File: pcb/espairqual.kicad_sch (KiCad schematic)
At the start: 29 parts, among them J1 24VAC, J2 PMSX003, J7 eflashy32, U1 BD9G101G, U2 ESP32-S2-WROVER, U3 AP1117-33

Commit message: hmm
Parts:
- added J3: USB_C_Receptacle_USB2.0, Connector_USB:USB_C_Receptacle_HRO_TYPE-C-31-M-12, symbol Connector:USB_C_Receptacle_USB2.0
- added R4, R7: 5k1, Resistor_SMD:R_0805_2012Metric, symbol Device:R_Small
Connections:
- net +5V: now also J3.A4 (VBUS), J3.A9 (VBUS), J3.B4 (VBUS), J3.B9 (VBUS)
- net GND: now also J3.A1 (GND), J3.A12 (GND), J3.B1 (GND), J3.B12 (GND), R4.2, R7.2
- new net: J3.A5 (CC1), R4.1
- new net: J3.B5 (CC2), R7.1
- no-connect marks 31 -> 38
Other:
- note added: "Alternate 5VDC Source"

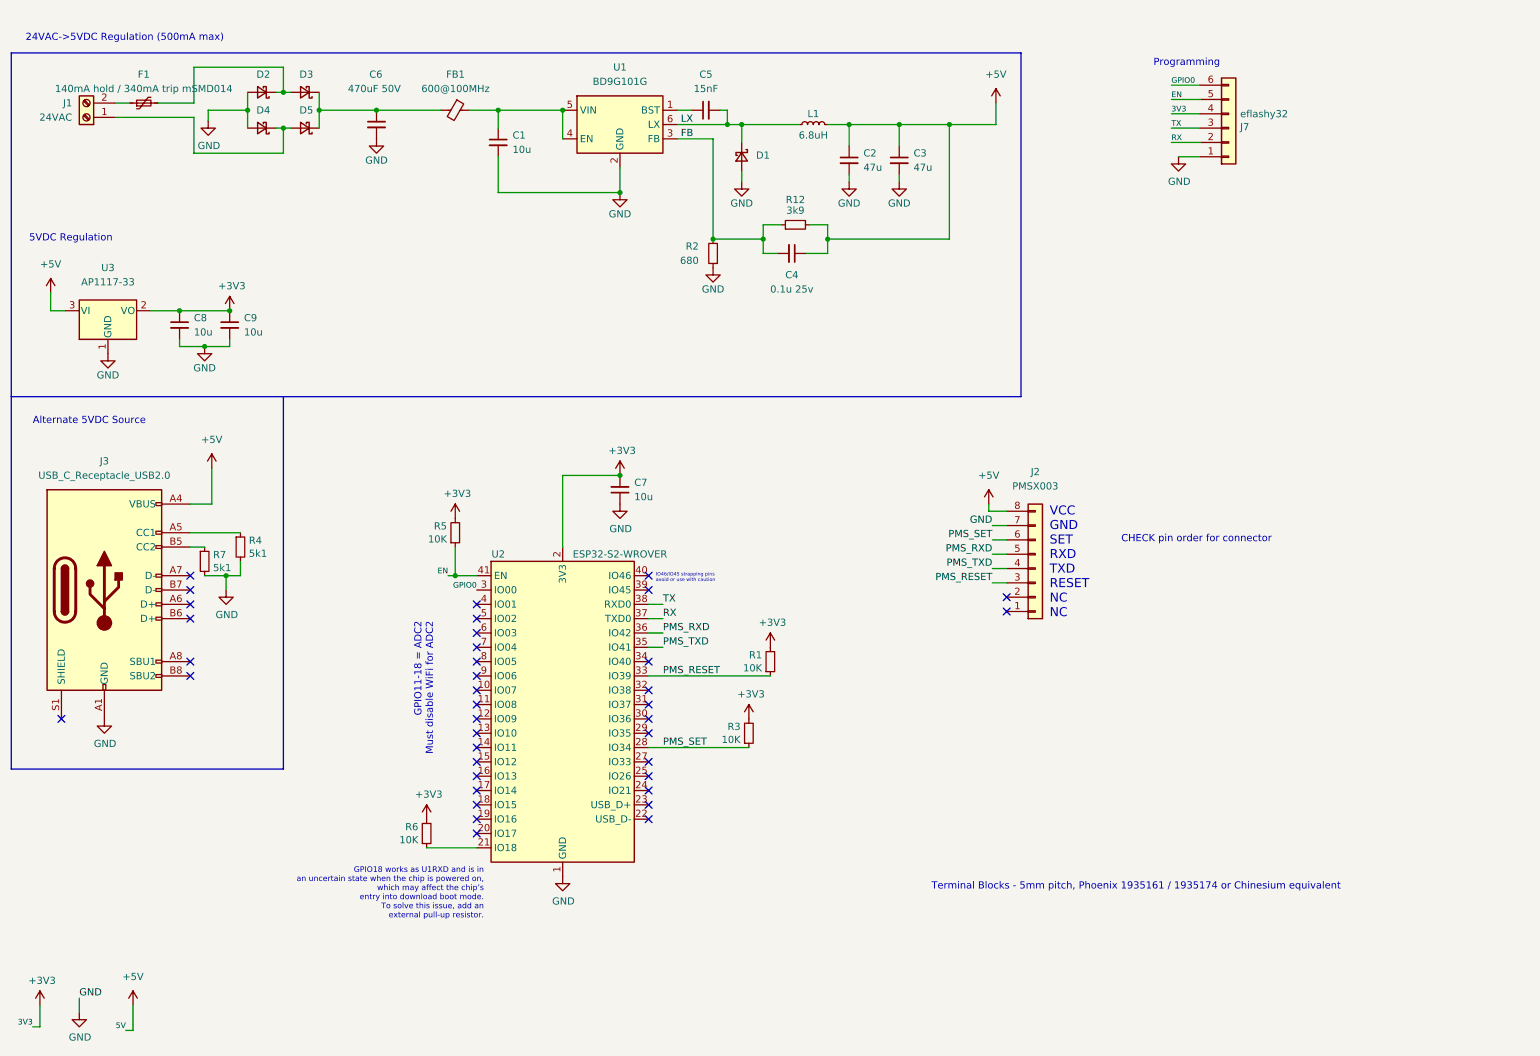
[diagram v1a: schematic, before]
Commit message: esp32 time
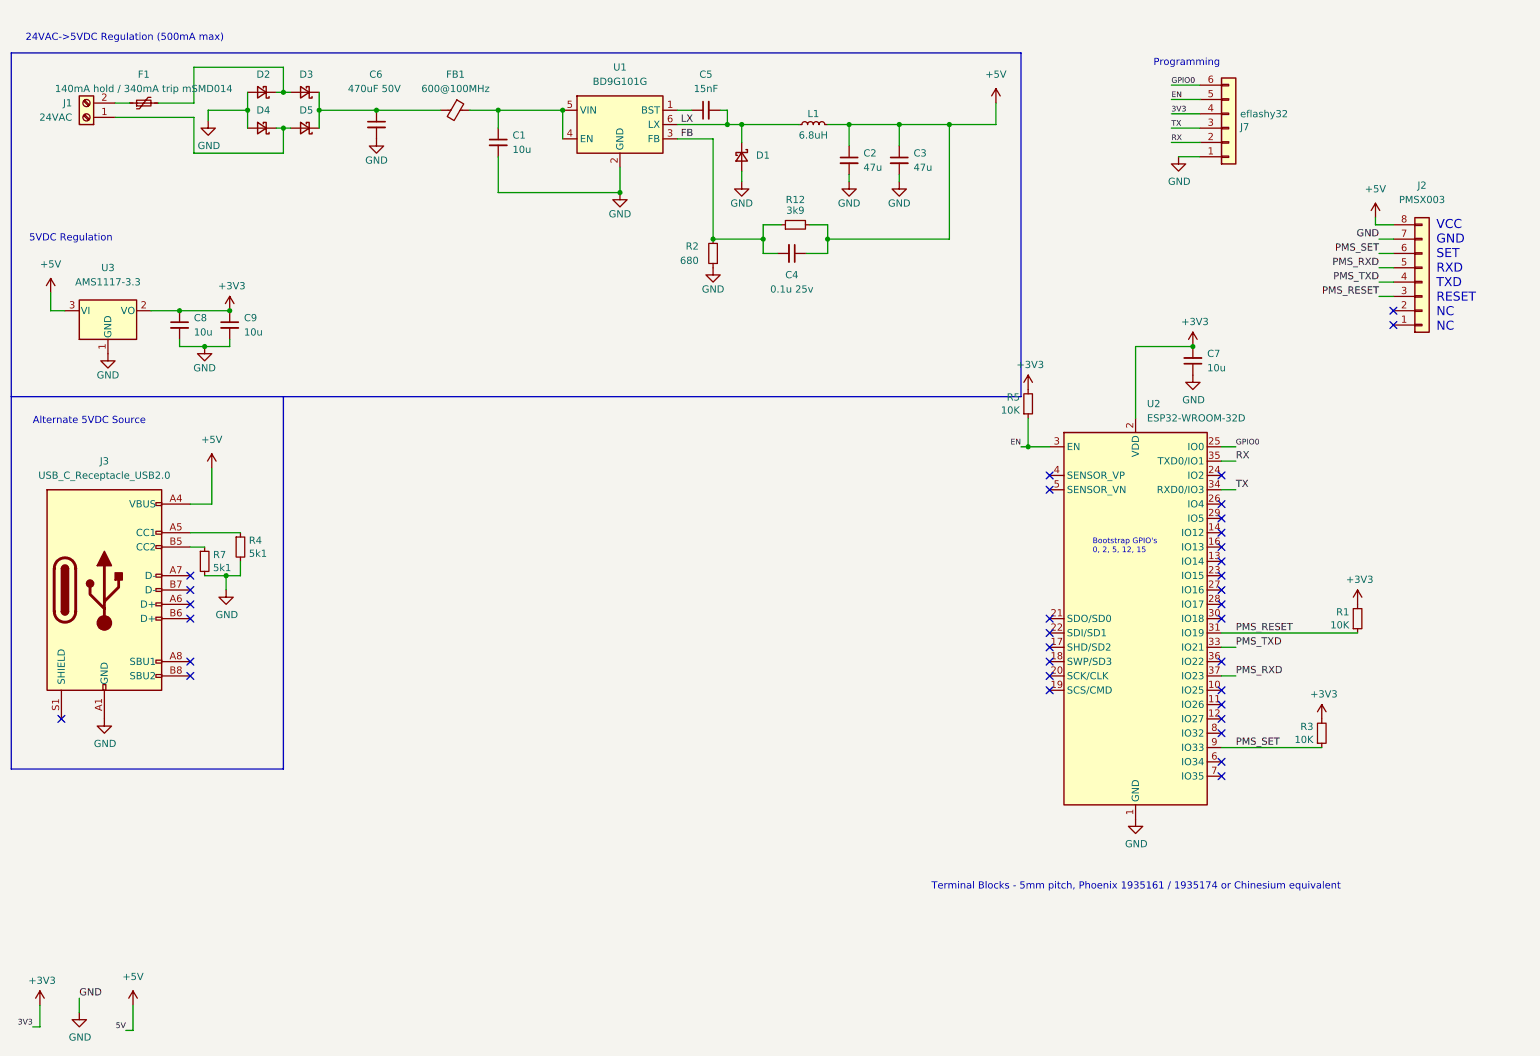
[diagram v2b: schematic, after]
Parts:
- removed R6: 10K, Resistor_SMD:R_0805_2012Metric, symbol Device:R_Small
- removed U2: ESP32-S2-WROVER, RF_Module:ESP32-S2-WROVER, symbol RF_Module:ESP32-S2-WROVER
- added U2: ESP32-WROOM-32D, RF_Module:ESP32-WROOM-32, symbol RF_Module:ESP32-WROOM-32D
- J1: LCSC a -> DNP
- J7: LCSC (none) -> DNP
- R1, R3, R5: footprint Resistor_SMD:R_0805_2012Metric -> Resistor_SMD:R_0402_1005Metric; LCSC C17414 -> C25086
- R12: footprint Resistor_SMD:R_0603_1608Metric -> Resistor_SMD:R_0402_1005Metric; LCSC C114616 -> C51721
- R2: footprint Resistor_SMD:R_0603_1608Metric -> Resistor_SMD:R_0402_1005Metric; LCSC C23228 -> C25130
- R4, R7: footprint Resistor_SMD:R_0805_2012Metric -> Resistor_SMD:R_0402_1005Metric; LCSC C27834 -> C25905
- U3: value AP1117-33 -> AMS1117-3.3; LCSC (none) -> C6186
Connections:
- net +3V3: now also U2.2 (VDD)
- net EN: now also U2.3 (EN)
- net GND: now also U2.1 (GND), U2.15 (GND), U2.38 (GND), U2.39 (GND)
- net GPIO0: now also U2.25 (IO0)
- net PMS_RESET: now also U2.31 (IO19)
- net PMS_RXD: now also U2.37 (IO23)
- net PMS_SET: now also U2.9 (IO33)
- net PMS_TXD: now also U2.33 (IO21)
- net RX: now also U2.35 (TXD0/IO1)
- net TX: now also U2.34 (RXD0/IO3)
- no-connect marks 38 -> 34
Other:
- note added: "Bootstrap GPIO's 0, 2, 5, 12, 15"
- note removed: "CHECK pin order for connector"
- note removed: "GPIO11-18 = ADC2 Must disable WiFi for ADC2"
- note removed: "GPIO18 works as U1RXD and is in an uncertain state when the chip is powered on, which may affect the chip’s entry into download boot mode. To solve this issue, add an external pull-up resistor."
- note removed: "IO46/IO45 strapping pins avoid or use with caution"
- moved on the sheet: C7, J2, R5

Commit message: caps
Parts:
- added C10, C11, C12: 10uF 50V, Capacitor_SMD:C_1206_3216Metric, symbol Device:C_Small
- C6: value 470uF 50V -> 10uF 50V; footprint Capacitor_SMD:CP_Elec_10x10 -> Capacitor_SMD:C_1206_3216Metric; LCSC C125977 -> C13585
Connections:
- net GND: now also C10.2, C11.2, C12.2
- net Vrec: now reaches C6.1, D3.1 (K), D5.1 (K), FB1.2
- net Vrec: now also C10.1, C11.1, C12.1
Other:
- moved on the sheet: FB1

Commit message: update workflow
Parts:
- removed C10, C11, C12: 10uF 50V, Capacitor_SMD:C_1206_3216Metric, symbol Device:C_Small
- added C10: 100uF 50V, Capacitor_THT:CP_Radial_D10.0mm_P5.00mm_P7.50mm, symbol Device:C_Polarized_Small
- added C16: 1uF, Capacitor_SMD:C_0603_1608Metric, symbol Device:C_Small
- added H1, H2, H3, H4: MountingHole, MountingHole:MountingHole_3.2mm_M3, symbol Mechanical:MountingHole
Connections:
- net EN: now also C16.2
- net GND: now also C10.2, C16.1
- net Vrec: now also C10.1
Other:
- moved on the sheet: C6

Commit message: changes
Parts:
- removed C16: 1uF, Capacitor_SMD:C_0603_1608Metric, symbol Device:C_Small
- removed C2, C3: 47u, Capacitor_SMD:C_1206_3216Metric, symbol Device:C_Small
- removed J3: USB_C_Receptacle_USB2.0, Connector_USB:USB_C_Receptacle_HRO_TYPE-C-31-M-12, symbol Connector:USB_C_Receptacle_USB2.0
- removed J7: eflashy32, Connector_PinHeader_2.54mm:PinHeader_1x06_P2.54mm_Vertical, symbol Connector_Generic:Conn_01x06
- removed R1, R3, R5: 10K, Resistor_SMD:R_0402_1005Metric, symbol Device:R_Small
- removed R4, R7: 5k1, Resistor_SMD:R_0402_1005Metric, symbol Device:R_Small
- removed U2: ESP32-WROOM-32D, RF_Module:ESP32-WROOM-32, symbol RF_Module:ESP32-WROOM-32D
- added C1 (x2): 10uF 50V, Capacitor_SMD:C_1206_3216Metric, symbol Device:C_Small
- added D6, D7: SS210, Diode_SMD:D_SMA, symbol Device:D_Schottky_Small
- added D8: PWR, LED_SMD:LED_0805_2012Metric, symbol Device:LED
- added J3: eflashy32, Connector_PinHeader_2.54mm:PinHeader_1x06_P2.54mm_Vertical, symbol Connector_Generic:Conn_01x06
- added J4: USBC, Connector_USB:USB_C_Receptacle_GCT_USB4105-xx-A_16P_TopMnt_Horizontal, symbol Connector:USB_C_Receptacle_USB2.0
- added J5: GCJA5, Connector_JST:JST_GH_SM05B-GHS-TB_1x05-1MP_P1.25mm_Horizontal, symbol Connector_Generic:Conn_01x05
- added J6: TEST, Connector_PinHeader_2.54mm:PinHeader_1x04_P2.54mm_Vertical, symbol Connector:Conn_01x04_Socket
- added J7: AUX, Connector_PinHeader_2.54mm:PinHeader_1x05_P2.54mm_Vertical_SMD_Pin1Left, symbol Connector:Conn_01x05_Pin
- added R5 (x6): 5k1, Resistor_SMD:R_0402_1005Metric, symbol Device:R_Small
- added R6: 680, Resistor_SMD:R_0402_1005Metric, symbol Device:R_Small
- added SW1: RESET, Button_Switch_SMD:SW_Push_1P1T_XKB_TS-1187A, symbol Switch:SW_SPST
- added TP1: +5V, TestPoint:TestPoint_Pad_D2.5mm, symbol Connector:TestPoint
- added TP2: GND, TestPoint:TestPoint_Pad_D2.5mm, symbol Connector:TestPoint
- added TP3: +3.3V, TestPoint:TestPoint_Pad_D2.5mm, symbol Connector:TestPoint
- added U4: ESP32-C3-MINI-1, Espressif:ESP32-C3-MINI-1, symbol Espressif:ESP32-C3-MINI-1
- C1, C7, C8, C9: value 10u -> 10uF 50V
- C10: footprint Capacitor_THT:CP_Radial_D10.0mm_P5.00mm_P7.50mm -> Capacitor_SMD:CP_Elec_8x10; LCSC (none) -> C445063
- L1: footprint Inductor_SMD:L_Sunlord_SWPA60xxS -> Inductor_SMD:L_Sunlord_SWPA5012S; LCSC C408337 -> C96909
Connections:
- net +3V3: now also C1.2, J3.4 (Pin_4), R5.1, R5.1, R5.1, TP3.1, U4.3 (3V3); no longer C7.2
- net +5V: now also D6.1 (K), D7.1 (K), D8.2 (A), J5.5 (Pin_5), TP1.1; no longer C4.1, L1.2, R12.2
- net EN: now also C1.2, J3.5 (Pin_5), R5.2, U4.8 (EN/CHIP_PU)
- net GND: now also C7.2, C1.1, C1.1, J3.1 (Pin_1), J4.A1 (GND), J4.A12 (GND), J4.B1 (GND), J4.B12 (GND), J5.2 (Pin_2), J6.1 (Pin_1), R5.2, R5.2, R6.2, SW1.2 (B), TP2.1, U4.1 (GND), U4.11 (GND), U4.14 (GND), U4.2 (GND), U4.36 (GND), U4.37 (GND), U4.38 (GND), U4.39 (GND), U4.40 (GND), U4.41 (GND), U4.42 (GND), U4.43 (GND), U4.44 (GND), U4.45 (GND), U4.46 (GND), U4.47 (GND), U4.48 (GND), U4.49 (GND), U4.50 (GND), U4.51 (GND), U4.52 (GND), U4.53 (GND); no longer C7.1
- net GPIO0: now also J3.6 (Pin_6), SW1.1 (A), U4.23 (GPIO9)
- net PMS_RXD: now also J3.2 (Pin_2), U4.31 (GPIO21/U0TXD)
- net PMS_TXD: now also J3.3 (Pin_3), U4.30 (GPIO20/U0RXD)
- net PMS_RESET renamed GPIO3
- net GPIO3: now also J7.5 (Pin_5), U4.6 (GPIO3/ADC1_CH3)
- net PMS_SET renamed GPIO5
- net GPIO5: now also J7.4 (Pin_4), U4.19 (GPIO5/ADC2_CH0)
- new net: C4.1, C7.1, D7.2 (A), L1.2, R12.2
- new net: R5.1, R5.2
- new net: D6.2 (A), J4.A4 (VBUS), J4.A9 (VBUS), J4.B4 (VBUS), J4.B9 (VBUS)
- new net: J4.A5 (CC1), R5.1
- new net: J4.B5 (CC2), R5.1
- new net: R5.2, U4.5 (GPIO2/ADC1_CH2)
- new net: D8.1 (K), R6.1
- new net: R5.2, U4.22 (GPIO8)
- new net D+: J4.A6 (D+), J4.B6 (D+), U4.27 (GPIO19/USB_D+)
- new net D-: J4.A7 (D-), J4.B7 (D-), U4.26 (GPIO18/USB_D-)
- new net GPIO10: J5.1 (Pin_1), J6.4 (Pin_4), J7.1 (Pin_1), U4.16 (GPIO10)
- new net GPIO6: J5.4 (Pin_4), J6.3 (Pin_3), J7.3 (Pin_3), U4.20 (GPIO6)
- new net GPIO7: J5.3 (Pin_3), J6.2 (Pin_2), J7.2 (Pin_2), U4.21 (GPIO7)
- no-connect marks 34 -> 8
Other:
- note added: "3.3VDC Regulation"
- note added: "Bootstrap 2, 8, 9"
- note added: "Bootstrapping - do not use GPIO9."
- note added: "Output(TX) from eflashy32"
- note added: "SDA/SCL are pulled high internally (10k) by GCJA5"
- note added: "USBC"
- note removed: "5VDC Regulation"
- note removed: "Alternate 5VDC Source"
- note removed: "Bootstrap GPIO's 0, 2, 5, 12, 15"
- moved on the sheet: J2

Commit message: tweak
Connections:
- net GND: now also J5.4 (Pin_4); no longer J5.2 (Pin_2)
- net GPIO6: now also J5.2 (Pin_2); no longer J5.4 (Pin_4)
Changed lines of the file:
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@@
     (effects (font (size 1.27 1.27)) (justify right bottom))
   )
-  (label "GND" (at 248.92 143.51 0) (fields_autoplaced)
+  (label "GND" (at 248.92 138.43 0) (fields_autoplaced)
     (effects (font (size 1.27 1.27)) (justify left bottom))
   )
@@
     (effects (font (size 1.27 1.27)) (justify left bottom))
   )
-  (label "PAN_SDA" (at 248.92 138.43 0) (fields_autoplaced)
+  (label "PAN_SDA" (at 248.92 143.51 0) (fields_autoplaced)
     (effects (font (size 1.27 1.27)) (justify left bottom))
   )

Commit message: touchup before fab
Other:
- note added: "Extra Breakout"
- note added: "Headers"
- moved on the sheet: C1, C10, C4, C5, C6, C7, C8, C9, D1, D2, D3, D4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

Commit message: updates
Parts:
- removed J6: TEST, Connector_PinHeader_2.54mm:PinHeader_1x04_P2.54mm_Vertical, symbol Connector:Conn_01x04_Socket
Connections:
- net PWR5V: now reaches D6.2 (A), J4.A4 (VBUS), J4.A9 (VBUS), J4.B4 (VBUS), J4.B9 (VBUS)
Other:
- moved on the sheet: D6
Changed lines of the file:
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@@
+    (stroke (width 0) (type default))
+  )
+  (wire (pts (xy 229.87 25.4) (xy 224.79 25.4))
     (stroke (width 0) (type default))
   )
@@
     (stroke (width 0) (type default))
   )
-  (wire (pts (xy 231.14 25.4) (xy 231.14 22.86))
+  (wire (pts (xy 234.95 25.4) (xy 234.95 22.86))
     (stroke (width 0) (type default))
   )
@@
     (stroke (width 0) (type default))
   )
-  (wire (pts (xy 229.87 25.4) (xy 231.14 25.4))
-    (stroke (width 0) (type default))
-  )
   (wire (pts (xy 142.24 29.21) (xy 144.78 29.21))
     (stroke (width 0) (type default))
@@
     (stroke (width 0) (type default))
   )
-  (rectangle (start 177.8 83.82) (end 213.36 162.56)
+  (rectangle (start 177.8 83.82) (end 213.36 142.24)
     (stroke (width 0) (type default))
     (fill (type none))
@@
     (effects (font (size 1.27 1.27)) (justify left bottom))
   )
-  (label "PAN_SDA" (at 195.58 153.67 180) (fields_autoplaced)
-    (effects (font (size 1.27 1.27)) (justify right bottom))
-  )
   (label "GPIO0" (at 111.76 161.29 0) (fields_autoplaced)
     (effects (font (size 1.27 1.27)) (justify left bottom))
@@
     (effects (font (size 1.27 1.27)) (justify left bottom))
   )
-  (label "PAN_SCL" (at 195.58 156.21 180) (fields_autoplaced)
-    (effects (font (size 1.27 1.27)) (justify right bottom))
-  )
   (label "PMS_SET" (at 111.76 151.13 0) (fields_autoplaced)
     (effects (font (size 1.27 1.27)) (justify left bottom))
@@
     (effects (font (size 1.27 1.27)) (justify left bottom))
   )
-  (label "GND" (at 195.58 158.75 180) (fields_autoplaced)
-    (effects (font (size 1.27 1.27)) (justify right bottom))
-  )
   (label "PROGRXD" (at 266.7 106.68 0) (fields_autoplaced)
+    (effects (font (size 1.27 1.27)) (justify left bottom))
+  )
+  (label "PWR5V" (at 224.79 25.4 0) (fields_autoplaced)
     (effects (font (size 1.27 1.27)) (justify left bottom))
   )
@@
   (label "PMS_TXD" (at 111.76 125.73 0) (fields_autoplaced)
     (effects (font (size 1.27 1.27)) (justify left bottom))
-  )
-  (label "PAN_UART_TXD" (at 195.58 151.13 180) (fields_autoplaced)
-    (effects (font (size 1.27 1.27)) (justify right bottom))
   )
   (label "EN" (at 52.07 118.11 0) (fields_autoplaced)
@@
         (path "/efdd8971-0318-4d66-ba3f-bc0ab1fdcf7e"
           (reference "#PWR03") (unit 1)
-        )
-      )
-    )
-  )
-  (symbol (lib_id "Connector:Conn_01x04_Socket") (at 200.66 156.21 0) (mirror x) (unit 1)
-    (in_bom yes) (on_board yes) (dnp no) (fields_autoplaced)
-    (property "Reference" "J6" (at 200.025 146.05 0)
-      (effects (font (size 1.27 1.27)))
-    )
-    (property "Value" "TEST" (at 200.025 148.59 0)
-      (effects (font (size 1.27 1.27)))
-    )
-    (property "Footprint" "Connector_PinHeader_2.54mm:PinHeader_1x04_P2.54mm_Vertical" (at 200.66 156.21 0)
-      (effects (font (size 1.27 1.27)) hide)
-    )
-    (property "Datasheet" "~" (at 200.66 156.21 0)
-      (effects (font (size 1.27 1.27)) hide)
-    )
-    (pin "1")
-    (pin "2")
-    (pin "3")
-    (pin "4")
-    (instances
-      (project "espairqual"
-        (path "/ac4e4760-4dbb-40a3-a395-65d3f7cc73da"
-          (reference "J6") (unit 1)
         )
       )
@@
     )
   )
-  (symbol (lib_id "Device:D_Schottky_Small") (at 227.33 25.4 180) (unit 1)
-    (in_bom yes) (on_board yes) (dnp no) (fields_autoplaced)
-    (property "Reference" "D6" (at 227.584 22.86 0)
-      (effects (font (size 1.27 1.27)))
-    )
-    (property "Value" "SS210" (at 227.584 21.59 0)
-      (effects (font (size 1.27 1.27)) hide)
-    )
-    (property "Footprint" "Diode_SMD:D_SMA" (at 227.33 25.4 90)
-      (effects (font (size 1.27 1.27)) hide)
-    )
-    (property "Datasheet" "~" (at 227.33 25.4 90)
-      (effects (font (size 1.27 1.27)) hide)
-    )
-    (property "LCSC" "C14996" (at 227.33 25.4 0)
+  (symbol (lib_id "Device:D_Schottky_Small") (at 232.41 25.4 180) (unit 1)
+    (in_bom yes) (on_board yes) (dnp no) (fields_autoplaced)
+    (property "Reference" "D6" (at 232.664 22.86 0)
+      (effects (font (size 1.27 1.27)))
+    )
+    (property "Value" "SS210" (at 232.664 21.59 0)
+      (effects (font (size 1.27 1.27)) hide)
+    )
+    (property "Footprint" "Diode_SMD:D_SMA" (at 232.41 25.4 90)
+      (effects (font (size 1.27 1.27)) hide)
+    )
+    (property "Datasheet" "~" (at 232.41 25.4 90)
+      (effects (font (size 1.27 1.27)) hide)
+    )
+    (property "LCSC" "C14996" (at 232.41 25.4 0)
       (effects (font (size 1.27 1.27)) hide)
     )
@@
     )
   )
-  (symbol (lib_id "power:+5V") (at 231.14 22.86 0) (unit 1)
-    (in_bom yes) (on_board yes) (dnp no) (fields_autoplaced)
-    (property "Reference" "#PWR017" (at 231.14 26.67 0)
-      (effects (font (size 1.27 1.27)) hide)
-    )
-    (property "Value" "+5V" (at 231.14 19.05 0)
-      (effects (font (size 1.27 1.27)))
-    )
-    (property "Footprint" "" (at 231.14 22.86 0)
-      (effects (font (size 1.27 1.27)) hide)
-    )
-    (property "Datasheet" "" (at 231.14 22.86 0)
-      (effects (font (size 1.27 1.27)) hide)
-    )
+  (symbol (lib_id "power:+5V") (at 234.95 22.86 0) (unit 1)
+    (in_bom yes) (on_board yes) (dnp no) (fields_autoplaced)
+    (property "Reference" "#PWR017" (at 234.95 26.67 0)
+      (effects (font (size 1.27 1.27)) hide)
+    )
+    (property "Value" "+5V" (at 234.95 19.05 0)
+      (effects (font (size 1.27 1.27)))
+    )
+    (property "Footprint" "" (at 234.95 22.86 0)
+      (effects (font (size 1.27 1.27)) hide)
+    )
+    (property "Datasheet" "" (at 234.95 22.86 0)
+      (effects (font (size 1.27 1.27)) hide)
+    )
